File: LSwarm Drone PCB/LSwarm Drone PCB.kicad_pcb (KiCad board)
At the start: 2 copper layers, 100 x 100 mm, 128 parts, among them J1 Conn_01x04_Pin, J2 USB_C_Receptacle_USB2.0_16P, J3 JST / BT2.0 Connector, J4 Conn_01x02_Pin, J5 Conn_01x02_Pin, J6 Conn_01x02_Pin, J7 Conn_01x02_Pin, Q1 AO3400A, Q2 AO3400A, Q3 AO3400A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

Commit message: sync
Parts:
- removed Q5: AO3401A, Package_TO_SOT_SMD:SOT-23
- removed R3: 1k, Resistor_SMD:R_0603_1608Metric
- removed U1: RP2350A, Package_DFN_QFN:QFN-60-1EP_7x7mm_P0.4mm_EP3.4x3.4mm
- removed U10: LSM6DSR, LSM6DSR:LGA-14L
- removed U11: BMP581, BMP581:BMP581
- removed U4: W25Q128JVS, Package_SO:SOIC-8_5.3x5.3mm_P1.27mm
- added 1k: 1k, Resistor_SMD:R_0603_1608Metric, F.Cu at (41.0, 41.0)
- added BARO: BMP581, BMP581:BMP581, F.Cu at (41.5, 45.0)
- added FLASH: W25Q128JVS, Package_SO:SOIC-8_5.3x5.3mm_P1.27mm, F.Cu at (47.5, 40.0)
- added IMU: LSM6DSR, LSM6DSR:LGA-14L, F.Cu at (41.0, 50.0)
- added Q7: AO3407A, easyeda2kicad:SOT-23-3_L2.9-W1.6-P1.90-LS2.8-BR, F.Cu at (177.9, 53.9)
- added RP2350A: RP2350A, Package_DFN_QFN:QFN-60-1EP_7x7mm_P0.4mm_EP3.4x3.4mm, F.Cu at (47.5, 49.0)
- moved S3 130.3 mm to (36.2, 39.0), turned to 180 degrees
- moved S2 127.8 mm to (47.4, 69.5), turned to 90 degrees
- moved J3 112.8 mm to (50.5, 77.0)
- moved L7 109.8 mm to (57.0, 46.5)
- moved J2 106.3 mm to (50.6, 21.4), turned to 180 degrees
- moved C15 106.0 mm to (37.5, 53.0), turned to 180 degrees
- moved C38 105.8 mm to (19.9, 66.0)
- moved SW1 105.0 mm to (21.5, 52.5), turned to -90 degrees
- moved J1 102.7 mm to (20.0, 79.5), turned to 90 degrees
- moved LED1 97.3 mm to (58.0, 64.5), turned to -90 degrees
- moved U12 96.6 mm to (66.9, 60.3)
- moved C20 96.3 mm to (32.0, 59.0), turned to 90 degrees
- moved L8 96.2 mm to (71.5, 38.5), turned to 90 degrees
- moved C19 96.1 mm to (32.0, 55.8), turned to -90 degrees
- moved U13 95.3 mm to (71.5, 60.2)
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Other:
- outline, holes or cut-outs redrawn
- copper layers 2 -> 4

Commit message: finished pcb layout
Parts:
- ESP32 BOOT: renamed from S6
- ESP32 EN: renamed from S5
- J3, LED3: moved to B.Cu
- LED1: renamed from LED2; moved to B.Cu
- LED3: renamed from LED4; moved to B.Cu
- LED4: renamed from LED5; moved to B.Cu
- moved J6 157.2 mm to (16.0, 89.5), turned to -90 degrees
- moved Q1 152.5 mm to (18.1, 22.0)
- moved LED4 151.1 mm to (15.0, 85.0), turned to 180 degrees
- moved Q3 146.7 mm to (23.5, 77.5)
- moved J4 144.0 mm to (14.8, 10.5), turned to -90 degrees
- moved LED1 142.7 mm to (15.0, 15.0), turned to 180 degrees
- moved D3 140.2 mm to (19.1, 77.0), turned to 90 degrees
- moved BUZZER2 140.1 mm to (34.7, 65.2)
- moved C47 134.6 mm to (21.5, 85.5), turned to 180 degrees
- moved R22 132.8 mm to (28.1, 79.5)
- moved R21 132.6 mm to (28.1, 76.5)
- moved D1 132.4 mm to (27.5, 22.0), turned to -90 degrees
- moved C72 127.9 mm to (54.0, 68.5)
- moved R12 126.7 mm to (22.1, 21.0)
- moved R11 126.0 mm to (22.1, 24.0)
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- renumbered U6 to ESP32, 1k to R3, RP2350A to RP2350, IMU to U10, BARO to U11
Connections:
- J1 pad 1: unconnected-(J1-Pin_1-Pad1) -> +3.3V
- J1 pad 2: unconnected-(J1-Pin_2-Pad2) -> GND
- J1 pad 3: unconnected-(J1-Pin_3-Pad3) -> RP2350_SWCLK
- J1 pad 4: unconnected-(J1-Pin_4-Pad4) -> RP2350_SWDIO
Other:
- outline, holes or cut-outs redrawn

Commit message: sync
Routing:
- net +5V: track 0.00 -> 248.1 mm, vias 0 -> 7
- net +3.3V: track 0.00 -> 175.7 mm, vias 0 -> 14
- net BATT_SW+: track 0.00 -> 167.5 mm, vias 0 -> 8
- net GND: track 0.00 -> 88.4 mm, vias 0 -> 82
- net Net-(LED2-DOUT): track 0.00 -> 81.3 mm
- net Net-(LED3-DOUT): track 0.00 -> 72.1 mm
- net Net-(LED4-DOUT): track 0.00 -> 69.4 mm, vias 0 -> 1
- net Net-(Q7-G): track 0.00 -> 58.5 mm, vias 0 -> 2
- net RP2350_GPIO_21: track 0.00 -> 49.8 mm, vias 0 -> 3
- net RP2350_GPIO_19: track 0.00 -> 44.1 mm, vias 0 -> 2
- net RP2350_GPIO_20: track 0.00 -> 43.5 mm, vias 0 -> 2
- net +1V1: track 0.00 -> 40.1 mm, vias 0 -> 3
- net RP2350_GPIO_22: track 0.00 -> 35.1 mm, vias 0 -> 2
- net RP2350_GPIO_26_ADC: track 0.00 -> 31.1 mm, vias 0 -> 3
- net RP2350_GPIO_24: track 0.00 -> 29.5 mm, vias 0 -> 2
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- added copper zone on In1.Cu, net GND

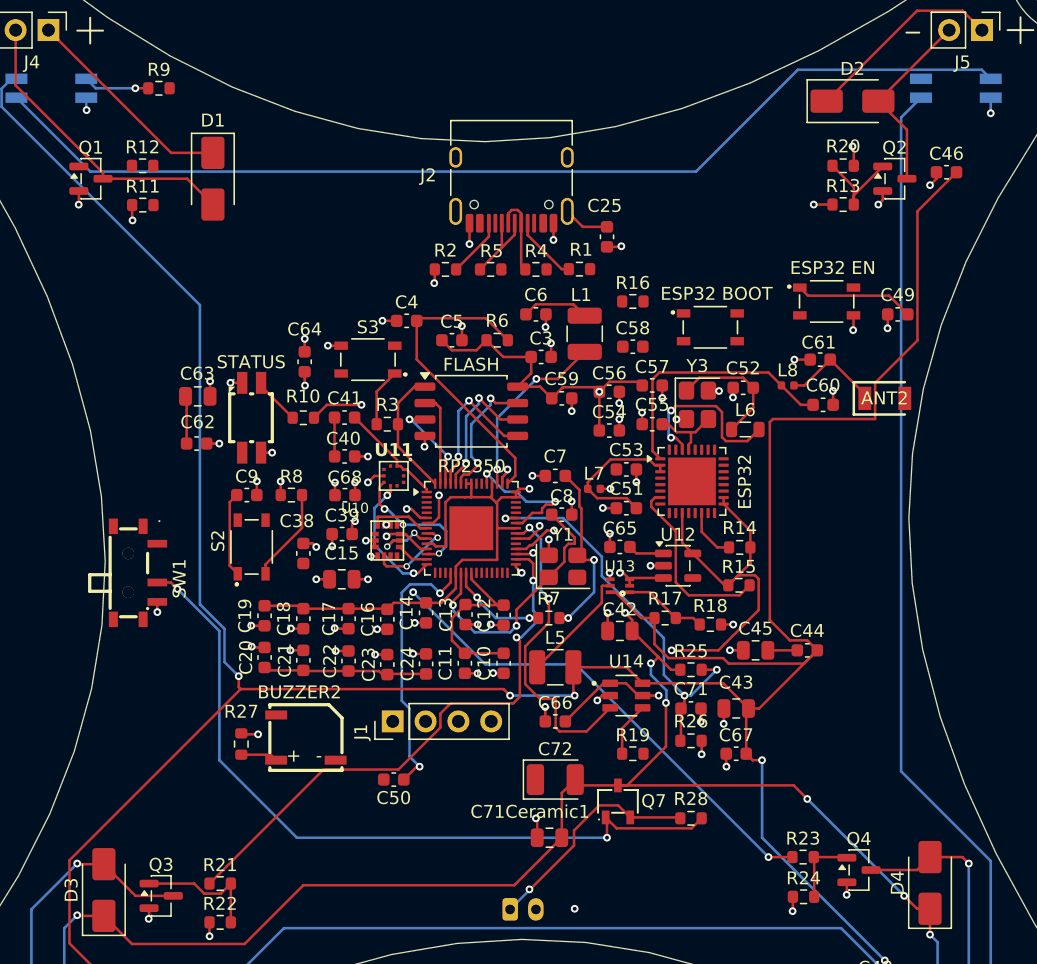
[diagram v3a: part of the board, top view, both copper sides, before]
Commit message: finished main wiring
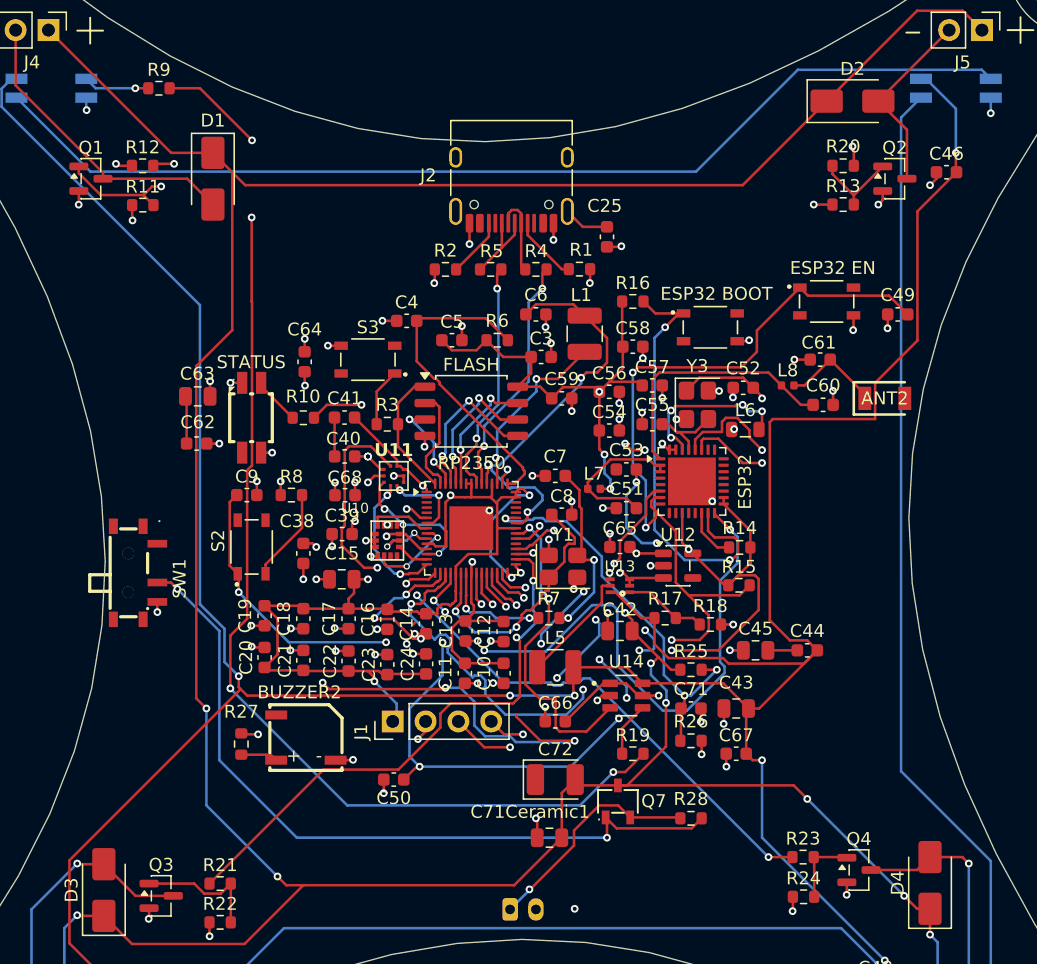
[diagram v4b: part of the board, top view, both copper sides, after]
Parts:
- moved C12 1.27 mm to (50.0, 57.0)
- moved C13 1.27 mm to (47.0, 57.0)
- moved C14 0.84 mm to (44.0, 56.4)
- moved C10 0.77 mm to (50.0, 60.3)
- moved C11 0.77 mm to (47.0, 60.3)
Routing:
- net BATT_SW+: track 167.5 -> 281.3 mm, vias 8 -> 11
- net RP2350_GPIO_18: track 0.00 -> 93.8 mm, vias 0 -> 2
- net RP2350_GPIO_25_5.5V: track 0.00 -> 88.6 mm, vias 0 -> 4
- net RP2350_GPIO_14: track 23.5 -> 94.4 mm, vias 0 -> 5
- net RP2350_GPIO_12: track 0.00 -> 67.9 mm, vias 0 -> 7
- net RP2350_GPIO_15: track 21.1 -> 88.0 mm, vias 2 -> 9
- net RP2350_GPIO_13: track 0.00 -> 57.4 mm, vias 0 -> 5
- net +3.3V: track 175.7 -> 229.3 mm, vias 14 -> 22
- net RP2350_GPIO_16: track 0.00 -> 41.9 mm, vias 0 -> 4
- net RP2350_GPIO_17: track 0.00 -> 41.4 mm, vias 0 -> 4
- net Net-(U1-RUN): track 6.58 -> 37.2 mm, vias 0 -> 4
- net +1V1: track 40.1 -> 66.5 mm, vias 3 -> 5
- net RP2350_SWCLK: track 0.00 -> 19.4 mm, vias 0 -> 2
- net RP2350_USB_DM: track 0.00 -> 18.9 mm, vias 0 -> 2
- net RP2350_USB_DP: track 0.00 -> 18.3 mm, vias 0 -> 2
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
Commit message: added graphics + other stuff
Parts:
- added GNU: Symbol_GNU-Logo_SilkscreenTop, Symbol:Symbol_GNU-Logo_SilkscreenTop, F.Cu at (70.3, 20.4)
- added dino: LOGO, dino:dino, F.Cu at (34.8, 24.4)
- added hackclub: LOGO, hackclub:hackclub, F.Cu at (37.0, 21.5)
- added logo: LOGO, mk1Logo:mk1Logo, F.Cu at (60.9, 78.0)
- moved R4 8.83 mm to (61.3, 28.3)
- moved R5 8.63 mm to (40.4, 28.5)
- moved R1 6.82 mm to (61.4, 25.0)
- moved R2 6.50 mm to (40.4, 25.0)
- moved J2 2.56 mm to (50.0, 23.9)
- moved D2 1.24 mm to (78.0, 15.2)
- moved C25 0.25 mm to (57.9, 26.7)
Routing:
- net BATT_SW+: track 281.3 -> 295.0 mm
- net Net-(J2-D+-PadA6): track 6.57 -> 15.9 mm
- net Net-(J2-D--PadA7): track 6.44 -> 14.9 mm
- net Net-(J2-CC2): track 4.62 -> 12.7 mm
- net Net-(J2-CC1): track 5.19 -> 12.5 mm
- net RP2350_USB_DP: track 18.3 -> 25.3 mm
- net RP2350_GPIO_12: track 67.9 -> 62.5 mm
- net +3.3V: track 229.3 -> 226.0 mm, vias 22 -> 21
- net GND: track 104.6 -> 101.9 mm, vias 94 -> 93
- net RP2350_GPIO_13: track 57.4 -> 59.9 mm
- net +5V: track 256.7 -> 255.3 mm
- net Net-(C7-Pad1): track 14.3 -> 13.3 mm
- net Net-(LED4-DOUT): track 69.4 -> 68.9 mm, vias 1 -> 0
- net Net-(U1-RUN): track 37.2 -> 37.1 mm, vias 4 -> 3
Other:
- board size 100 x 100 mm -> 100 x 99.8 mm
- board text added: "Unit __"

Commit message: sync
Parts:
- moved SW1 1.39 mm to (22.9, 52.5)
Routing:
- net RP2350_USB_DM: track 18.4 -> 27.5 mm
- net Net-(Q7-G): track 58.4 -> 57.2 mm
- net Net-(J2-CC1): track 12.5 -> 13.7 mm
- net GND: track 101.9 -> 101.1 mm, vias 93 -> 92
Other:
- board text added: "OFF"
- board text added: "ON"
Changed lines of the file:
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@@
 	(footprint "easyeda2kicad:SW-TH_MSK12C02"
 		(layer "F.Cu")
-		(at 21.5 52.5 -90)
+		(at 22.891365 52.463391 -90)
 		(property "Reference" "SW1"
-			(at 0.450761 -3.427296 90)
+			(at -5.442434 0.317839 0)
 			(layer "F.SilkS")
 			(effects
@@
 		(at 41 50 -90)
 		(property "Reference" "U10"
-			(at -2.300853 0.155548 0)
+			(at -2.5 0 0)
 			(layer "F.SilkS")
 			(effects
@@
 		(tags "capacitor")
 		(property "Reference" "C6"
-			(at 0 1.5 0)
+			(at 1 1 0)
 			(layer "F.SilkS")
 			(effects
@@
 		(layer "Edge.Cuts")
 	)
+	(gr_text "ON"
+		(at 20 50 90)
+		(layer "F.SilkS")
+		(effects
+			(font
+				(size 1 1)
+				(thickness 0.15)
+			)
+		)
+	)
+	(gr_text "OFF"
+		(at 20 55.5 90)
+		(layer "F.SilkS")
+		(effects
+			(font
+				(size 1 1)
+				(thickness 0.15)
+			)
+		)
+	)
 	(gr_text "Unit __"
 		(at 35.5 80.5 0)
@@
 	)
 	(segment
-		(start 23.2 55.538168)
-		(end 23.202018 55.540186)
-		(width 0.2)
-		(layer "F.Cu")
-		(net "GND")
-	)
-	(segment
 		(start 62.275 38.966939)
 		(end 62.279905 38.971844)
@@
 	)
 	(segment
-		(start 23.2 54.75)
-		(end 23.2 55.538168)
-		(width 0.2)
-		(layer "F.Cu")
-		(net "GND")
-	)
-	(segment
 		(start 53.25 27.926118)
 		(end 53.25 29.213666)
@@
 	)
 	(via
-		(at 23.202018 55.540186)
-		(size 0.6)
-		(drill 0.3)
-		(layers "F.Cu" "B.Cu")
-		(net "GND")
-	)
-	(via
 		(at 58.218153 49.464184)
 		(size 0.6)
@@
 	)
 	(segment
-		(start 24.75 53.75)
-		(end 24.25 53.25)
-		(width 0.2)
-		(layer "F.Cu")
-		(net "Net-(Q7-G)")
-	)
-	(segment
 		(start 64.55 72.275)
 		(end 58.740601 72.275)
@@
 		(net "Net-(Q7-G)")
 	)
-	(segment
-		(start 24.25 53.25)
-		(end 23.2 53.25)
-		(width 0.2)
-		(layer "F.Cu")
-		(net "Net-(Q7-G)")
-	)
 	(via
-		(at 24.75 53.75)
+		(at 24.591365 53.213391)
 		(size 0.6)
 		(drill 0.3)
@@
 	)
 	(segment
+		(start 28 57)
+		(end 24.591365 53.591365)
+		(width 0.2)
+		(layer "B.Cu")
+		(net "Net-(Q7-G)")
+	)
+	(segment
+		(start 24.591365 53.591365)
+		(end 24.591365 53.213391)
+		(width 0.2)
+		(layer "B.Cu")
+		(net "Net-(Q7-G)")
+	)
+	(segment
 		(start 28 67)
 		(end 34 73)
@@
 	)
 	(segment
-		(start 24.75 53.75)
-		(end 28 57)
-		(width 0.2)
-		(layer "B.Cu")
-		(net "Net-(Q7-G)")
-	)
-	(segment
 		(start 52 77)
 		(end 52.05 77)
@@
 	)
 	(segment
+		(start 23.2 55.538168)
+		(end 23.202018 55.540186)
+		(width 0.2)
+		(layer "F.Cu")
+		(net "unconnected-(SW1-Pad4)")
+	)
+	(segment
 		(start 67.5 51.509712)
 		(end 67.658253 51.509712)
@@
 	)
 	(segment
-		(start 50.75 27.926118)
-		(end 50.75 28.86)
+		(start 58.422468 30.376722)
+		(end 60.477898 28.321292)
 		(width 0.2)
 		(layer "F.Cu")
@@
 	(segment
 		(start 50.75 27.926118)
-		(end 50.75 27.168708)
+		(end 50.75 28.86)
 		(width 0.2)
 		(layer "F.Cu")
@@
 	)
 	(segment
-		(start 49.75 27.168708)
-		(end 49.75 27.926118)
+		(start 50.75 27.926118)
+		(end 50.75 27.168708)
 		(width 0.2)
 		(layer "F.Cu")
@@
 	)
 	(segment
-		(start 52.266722 30.376722)
-		(end 58.422468 30.376722)
+		(start 50.75 28.86)
+		(end 52.266722 30.376722)
 		(width 0.2)
 		(layer "F.Cu")
@@
 	)
 	(segment
-		(start 50.48241 26.901118)
-		(end 50.01759 26.901118)
+		(start 49.75 27.168708)
+		(end 49.75 27.926118)
 		(width 0.2)
 		(layer "F.Cu")
@@
 	)
 	(segment
-		(start 50.01759 26.901118)
-		(end 49.75 27.168708)
+		(start 50.48241 26.901118)
+		(end 50.01759 26.901118)
 		(width 0.2)
 		(layer "F.Cu")
@@
 	)
 	(segment
-		(start 50.75 27.168708)
-		(end 50.48241 26.901118)
+		(start 52.266722 30.376722)
+		(end 58.422468 30.376722)
 		(width 0.2)
 		(layer "F.Cu")
@@
 	)
 	(segment
-		(start 58.422468 30.376722)
-		(end 60.477898 28.321292)
+		(start 50.01759 26.901118)
+		(end 49.75 27.168708)
 		(width 0.2)
 		(layer "F.Cu")
@@
 	)
 	(segment
-		(start 50.75 28.86)
-		(end 52.266722 30.376722)
+		(start 50.75 27.168708)
+		(end 50.48241 26.901118)
 		(width 0.2)
 		(layer "F.Cu")
@@
 	)
 	(segment
+		(start 48.500001 42.685563)
+		(end 48.500001 41.131371)
+		(width 0.2)
+		(layer "B.Cu")
+		(net "RP2350_USB_DM")
+	)
+	(segment
+		(start 51.936027 31.563973)
+		(end 53 30.5)
+		(width 0.2)
+		(layer "B.Cu")
+		(net "RP2350_USB_DM")
+	)
+	(segment
+		(start 61.105308 30.5)
+		(end 61.802898 29.80241)
+		(width 0.2)
+		(layer "B.Cu")
+		(net "RP2350_USB_DM")
+	)
+	(segment
 		(start 51.936027 37.695345)
 		(end 51.936027 31.563973)
@@
 	)
 	(segment
-		(start 51.936027 31.563973)
-		(end 53 30.5)
+		(start 53 30.5)
+		(end 61.105308 30.5)
 		(width 0.2)
 		(layer "B.Cu")
@@
 	)
 	(segment
-		(start 48.500001 42.685563)
-		(end 48.500001 41.131371)
-		(width 0.2)
-		(layer "B.Cu")
-		(net "RP2350_USB_DM")
-	)
-	(segment
 		(start 29.350907 46.482823)
 		(end 28.8 47.03373)
@@
 	)
 	(segment
-		(start 52.384491 29.818019)
-		(end 54.348285 29.818019)
+		(start 51.25 27.926118)
+		(end 51.25 28.683528)
 		(width 0.2)
 		(layer "F.Cu")
@@
 	)
 	(segment
-		(start 57.416304 26.75)
-		(end 58.815 26.75)
+		(start 54.348285 29.818019)
+		(end 55.666304 28.5)
 		(width 0.2)
 		(layer "F.Cu")
@@
 	)
 	(segment
-		(start 54.348285 29.818019)
-		(end 57.416304 26.75)
+		(start 59 28.5)
+		(end 60.565 26.935)
 		(width 0.2)
 		(layer "F.Cu")
@@
 	)
 	(segment
-		(start 51.25 27.926118)
-		(end 51.25 28.683528)
+		(start 55.666304 28.5)
+		(end 59 28.5)
 		(width 0.2)
 		(layer "F.Cu")
@@
 	)
 	(segment
-		(start 58.815 26.75)
+		(start 60.565 26.935)
 		(end 60.565 25)
 		(width 0.2)
@@
 	)
 	(segment
+		(start 52.384491 29.818019)
+		(end 54.348285 29.818019)
+		(width 0.2)
+		(layer "F.Cu")
+		(net "Net-(J2-CC1)")
+	)
+	(segment
 		(start 37.7 48.851304)
 		(end 37.475 49.076304)
@@
 	)
 	(segment
+		(start 40.775 48.1625)
+		(end 41.725 48.1625)
+		(width 0.2)
+		(layer "F.Cu")
+		(net "RP2350_GPIO_5")
+	)
+	(segment
 		(start 40.275 48.1625)
+		(end 40.775 48.1625)
+		(width 0.2)
+		(layer "F.Cu")
+		(net "RP2350_GPIO_5")
+	)
+	(segment
+		(start 41.725 48.1625)
 		(end 42.66614 48.1625)
 		(width 0.2)
@@
 	(segment
 		(start 40.25 48.78)
-		(end 40.25 48.1875)
+		(end 40.275 48.755)
 		(width 0.2)
 		(layer "F.Cu")
@@
 	)
 	(segment
-		(start 43.55364 49.05)
-		(end 44.05 49.05)
+		(start 42.66614 48.1625)
+		(end 43.55364 49.05)
 		(width 0.2)
 		(layer "F.Cu")
@@
 	)
 	(segment
-		(start 40.25 48.1875)
+		(start 40.275 48.755)
 		(end 40.275 48.1625)
 		(width 0.2)
@@
 	)
 	(segment
-		(start 42.66614 48.1625)
-		(end 43.55364 49.05)
+		(start 43.55364 49.05)
+		(end 44.05 49.05)
 		(width 0.2)
 		(layer "F.Cu")
@@
 		)
 		(min_thickness 0.25)
-		(fill
+		(fill yes
 			(thermal_gap 0.5)
 			(thermal_bridge_width 0.5)

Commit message: sync
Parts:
- removed ANT2: ANT3216LL00R2400A, ANT3216LL00R2400A:ANTC3216X135N
- removed C25: 10nF, Capacitor_SMD:C_0603_1608Metric
- removed ESP32 BOOT: SKRPACE010, SKRPACE010:SW_SKRPACE010
- removed ESP32 EN: SKRPACE010, SKRPACE010:SW_SKRPACE010
- removed J2: USB_C_Receptacle_USB2.0_16P, Connector_USB:USB_C_Receptacle_HRO_TYPE-C-31-M-12
- removed R1, R2: 5.1k, Resistor_SMD:R_0603_1608Metric
- removed R4, R5: 27, Resistor_SMD:R_0603_1608Metric
- removed S2, S3: SKRPACE010, SKRPACE010:SW_SKRPACE010
- removed U10: LSM6DSR, LSM6DSR:LGA-14L
- removed U11: BMP581, BMP581:BMP581
- removed U13: TPS61023DRLR, TPS61023DRLR:SOT563-ORI
- removed U14: SN74LVC1T45DBVR, SN74LVC1T45DBVR:SOT95P280X145-6N
- added C26: 10nF, Capacitor_SMD:C_0603_1608Metric, F.Cu at (40.5, 25.0)
- added JP1: U.FL-R-SMT-1, easyeda2kicad:RF-SMD_FRF05002-JSS103M, F.Cu at (73.5, 47.2)
- added R29: 10k, Resistor_SMD:R_0603_1608Metric, F.Cu at (27.5, 45.0)
- added R30: 10k, Resistor_SMD:R_0603_1608Metric, F.Cu at (34.1, 43.8)
- added R31: 10k, Resistor_SMD:R_0603_1608Metric, F.Cu at (40.7, 53.8)
- added R32: 5.1k, Resistor_SMD:R_0603_1608Metric, F.Cu at (44.0, 28.5)
- added R33: 5.1k, Resistor_SMD:R_0603_1608Metric, F.Cu at (56.5, 28.5)
- added R34: 27, Resistor_SMD:R_0603_1608Metric, F.Cu at (61.0, 28.5)
- added R35: 27, Resistor_SMD:R_0603_1608Metric, F.Cu at (40.5, 28.5)
- added SW2: SKRPACE010, easyeda2kicad:KEY-SMD_4P-L4.2-W3.2-P2.20-LS4.6, F.Cu at (30.5, 50.5)
- added SW3: SKRPACE010, easyeda2kicad:KEY-SMD_4P-L4.2-W3.2-P2.20-LS4.6, F.Cu at (39.5, 36.0)
- added SW4: SKRPACE010, easyeda2kicad:KEY-SMD_4P-L4.2-W3.2-P2.20-LS4.6, F.Cu at (74.0, 29.8)
- added SW5: SKRPACE010, easyeda2kicad:KEY-SMD_4P-L4.2-W3.2-P2.20-LS4.6, F.Cu at (66.0, 33.5)
- added U1: LSM6DSRTR, easyeda2kicad:LGA-14_L3.0-W2.5-P0.50-BR, F.Cu at (41.0, 50.0)
- added U3: TPS61023DRLR, easyeda2kicad:SOT-563_L1.6-W1.2-P0.50-LS1.6-BR, F.Cu at (59.0, 53.5)
- added U4: SN74LVC1T45DBVR, easyeda2kicad:SOT-23-6_L2.9-W1.6-P0.95-LS2.8-BR, F.Cu at (59.5, 62.0)
- added U5: BMP581, easyeda2kicad:LGA-10_L2.0-W2.0-P0.50-TL_BMP581, F.Cu at (41.5, 45.0)
- added USB1: USB-TYPE-C-018, easyeda2kicad:USB-C_SMD-TYPE-C-31-M-12, F.Cu at (50.2, 25.0)
- moved C60 5.26 mm to (72.0, 44.0)
- moved C61 4.51 mm to (74.7, 40.5)
- moved L8 4.51 mm to (72.2, 42.5)
- moved C49 2.01 mm to (79.5, 30.8)
- moved GNU 0.74 mm to (69.5, 20.3)
- turned D2 to 180 degrees
- turned R18 to 180 degrees
- renumbered FLASH to FLASH1, LED3 to LED2, LED1 to STATUS1
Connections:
- C40 pad 2: GND -> +3.3V
- C41 pad 1: +3.3V -> GND
- R17 pad 1: Net-(U13-FB) -> Net-(U3-FB)
- R18 pad 1: Net-(U13-FB) -> GND
- R18 pad 2: GND -> Net-(U3-FB)
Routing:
- net Net-(C26-Pad2): track 0.00 -> 22.8 mm
- net Net-(USB1-DP1): track 0.00 -> 16.8 mm
- net Net-(J2-D+-PadA6): track 15.9 -> 0.00 mm
- net Net-(USB1-DN1): track 0.00 -> 15.3 mm
- net RP2350_GPIO_5: track 4.77 -> 20.0 mm, vias 0 -> 4
- net Net-(J2-D--PadA7): track 14.9 -> 0.00 mm
- net BATT_SW+: track 295.0 -> 281.0 mm
- net Net-(J2-CC1): track 13.7 -> 0.00 mm
- net Net-(J2-CC2): track 12.7 -> 0.00 mm
- net Net-(USB1-CC1): track 0.00 -> 10.7 mm, vias 0 -> 2
- net Net-(USB1-CC2): track 0.00 -> 9.33 mm, vias 0 -> 2
- net RP2350_GPIO_11: track 10.8 -> 18.6 mm, vias 2 -> 3
- net Net-(D2-A): track 14.4 -> 21.7 mm
- net Net-(U3-FB): track 0.00 -> 6.46 mm
- net Net-(U13-FB): track 6.46 -> 0.00 mm
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
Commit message: sync
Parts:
- moved logo 17.3 mm to (74.9, 67.8)
- moved D1 10.0 mm to (17.5, 21.5)
- moved R11 5.28 mm to (26.0, 20.5), turned to 180 degrees
- moved R12 4.66 mm to (26.0, 23.5), turned to 180 degrees
- moved Q1 3.47 mm to (21.5, 22.5), turned to 180 degrees
- moved C44 3.20 mm to (71.0, 60.5)
- moved JP1 1.76 mm to (73.5, 49.0)
- moved C71C 1.57 mm to (54.0, 71.5)
- moved Q2 0.72 mm to (79.6, 22.0)
- moved R13 0.72 mm to (75.6, 24.0)
- moved R20 0.72 mm to (75.6, 21.0), turned to 0 degrees
- moved C67 0.50 mm to (68.5, 66.5)
- turned R21 to 180 degrees
- turned R22 to 180 degrees
- renumbered C71Ceramic1 to C71C
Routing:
- net +5V: track 249.5 -> 319.5 mm, vias 8 -> 10
- net BATT_SW+: track 281.0 -> 346.7 mm, vias 11 -> 12
- net GND: track 106.9 -> 123.0 mm, vias 95 -> 102
- net Net-(Q1-G): track 12.6 -> 5.76 mm, vias 2 -> 0
- net Net-(Q7-G): track 61.9 -> 56.0 mm, vias 2 -> 3
- net RP2350_GPIO_18: track 93.8 -> 89.0 mm
- net Net-(D1-A): track 23.6 -> 19.4 mm
- net BATT+: track 19.6 -> 16.3 mm
- net RP2350_GPIO_25_5.5V: track 88.6 -> 91.7 mm
- net Net-(D4-A): track 23.2 -> 20.7 mm, vias 1 -> 0
- net Net-(Q3-G): track 9.97 -> 7.68 mm
- net Net-(JP1-SIG): track 9.06 -> 10.8 mm
- net RP2350_GPIO_16: track 41.9 -> 43.6 mm
- net Net-(D2-A): track 21.7 -> 20.1 mm
- net Net-(Q2-G): track 6.85 -> 5.26 mm
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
